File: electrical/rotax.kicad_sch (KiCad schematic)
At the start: 14 parts

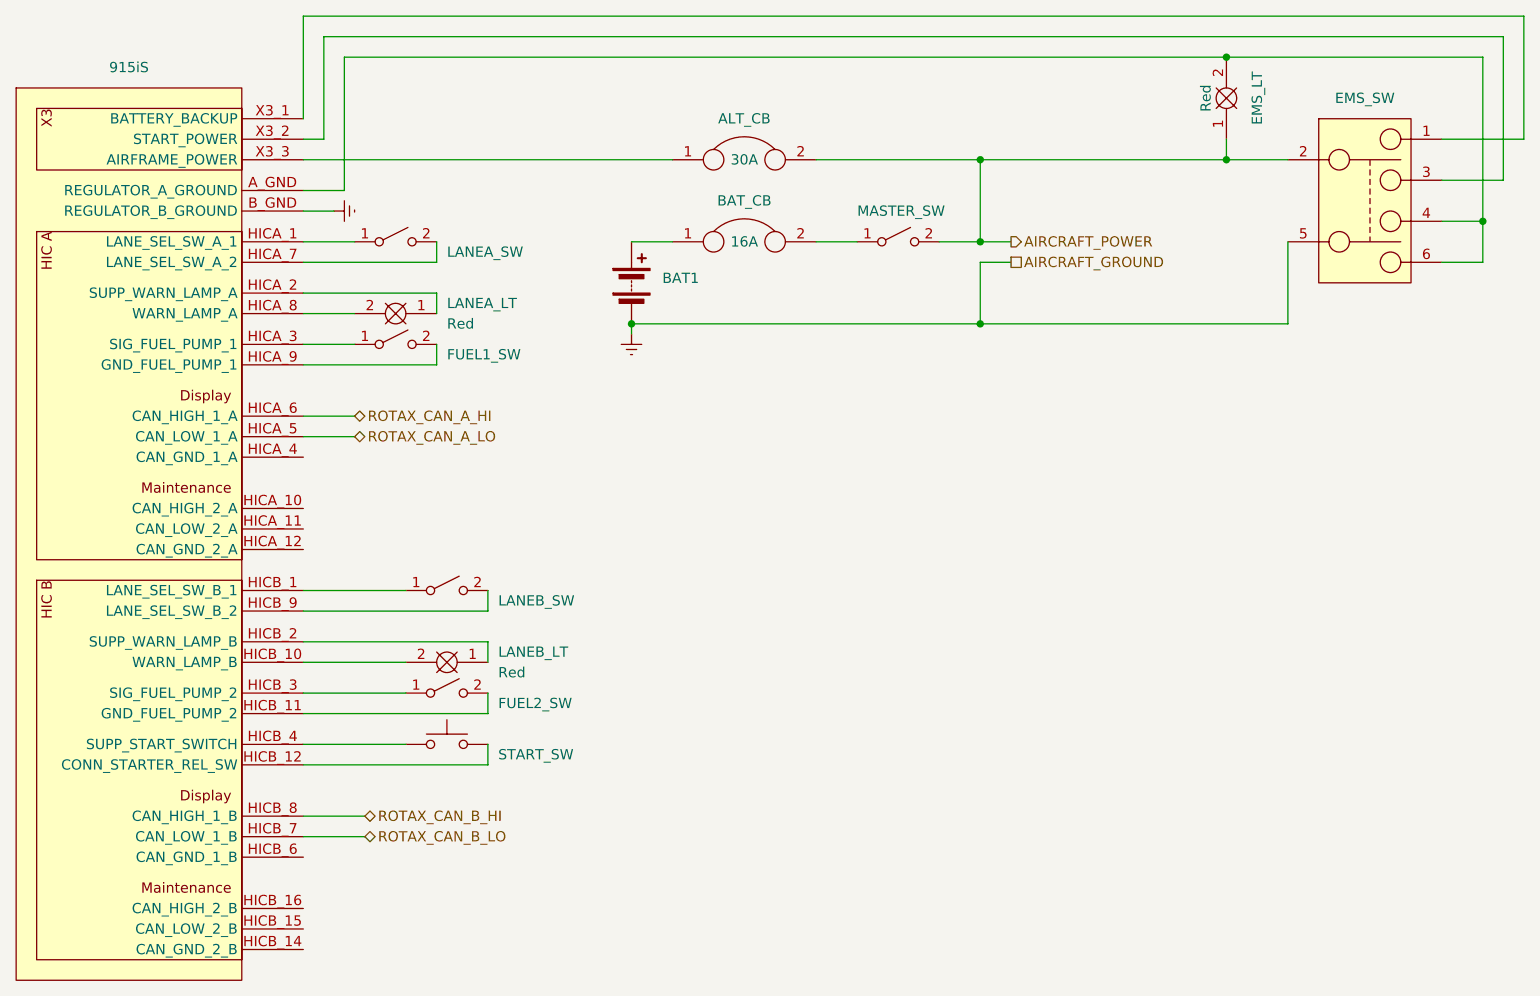
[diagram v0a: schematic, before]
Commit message: Changed grounds and canbuses to be in/out when applicable.
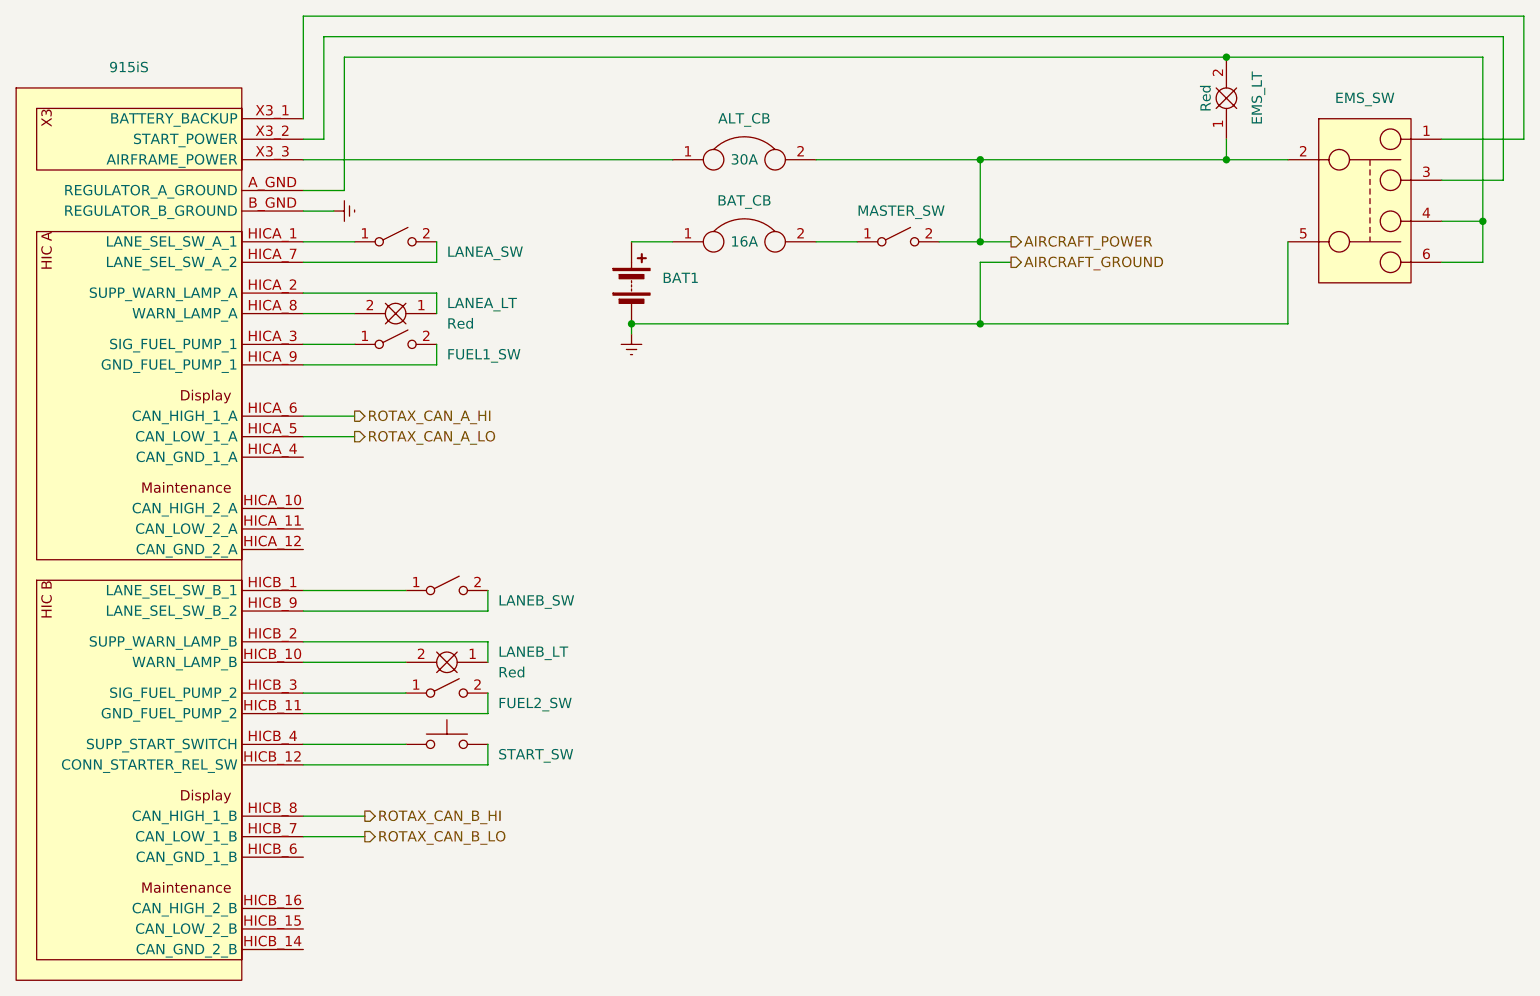
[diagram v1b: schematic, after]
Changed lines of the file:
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@@
     (stroke (width 0) (type default))
   )
-  (hierarchical_label "ROTAX_CAN_B_LO" (shape bidirectional) (at 95.25 153.67 0) (fields_autoplaced)
+  (hierarchical_label "ROTAX_CAN_B_LO" (shape output) (at 95.25 153.67 0) (fields_autoplaced)
     (effects (font (size 1.27 1.27)) (justify left))
   )
-  (hierarchical_label "ROTAX_CAN_A_LO" (shape bidirectional) (at 93.98 104.14 0) (fields_autoplaced)
+  (hierarchical_label "ROTAX_CAN_A_LO" (shape output) (at 93.98 104.14 0) (fields_autoplaced)
     (effects (font (size 1.27 1.27)) (justify left))
   )
-  (hierarchical_label "ROTAX_CAN_B_HI" (shape bidirectional) (at 95.25 151.13 0) (fields_autoplaced)
+  (hierarchical_label "ROTAX_CAN_B_HI" (shape output) (at 95.25 151.13 0) (fields_autoplaced)
     (effects (font (size 1.27 1.27)) (justify left))
   )
@@
     (effects (font (size 1.27 1.27)) (justify left))
   )
-  (hierarchical_label "ROTAX_CAN_A_HI" (shape bidirectional) (at 93.98 101.6 0) (fields_autoplaced)
+  (hierarchical_label "ROTAX_CAN_A_HI" (shape output) (at 93.98 101.6 0) (fields_autoplaced)
     (effects (font (size 1.27 1.27)) (justify left))
   )
-  (hierarchical_label "AIRCRAFT_GROUND" (shape passive) (at 175.26 82.55 0) (fields_autoplaced)
+  (hierarchical_label "AIRCRAFT_GROUND" (shape output) (at 175.26 82.55 0) (fields_autoplaced)
     (effects (font (size 1.27 1.27)) (justify left))
   )

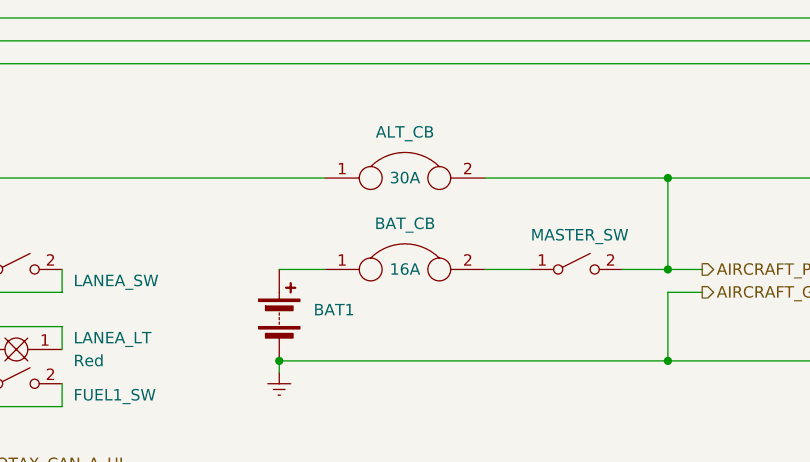
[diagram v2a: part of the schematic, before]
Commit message: Changed rotax power to 25A.
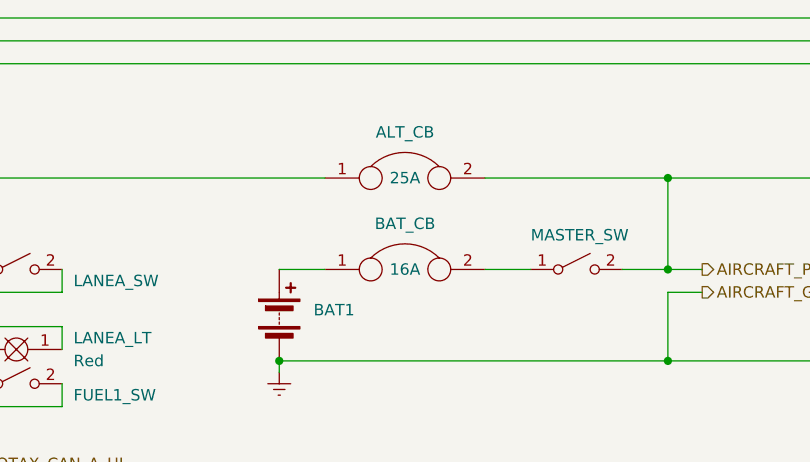
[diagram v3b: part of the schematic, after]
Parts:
- ALT_CB: value 30A -> 25A
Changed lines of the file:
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@@
       (effects (font (size 1.27 1.27)))
     )
-    (property "Value" "30A" (at 142.24 69.85 0)
+    (property "Value" "25A" (at 142.24 69.85 0)
       (effects (font (size 1.27 1.27)))
     )
